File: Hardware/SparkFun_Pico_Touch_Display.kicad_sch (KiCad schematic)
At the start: 53 parts, among them J1 Conn_01x20, J2 Conn_01x20, J3 Conn_02x10_SMD_RA, J4 Conn_1x21_FPC, J5 Qwiic_Vertical, J6 microSD, Q1 RE1C002UNTCL, SW1 SMD_4.6x2.8mm_h2.5mm, U1 2" LCD-TFT 240x320, U2 PCA9554PW

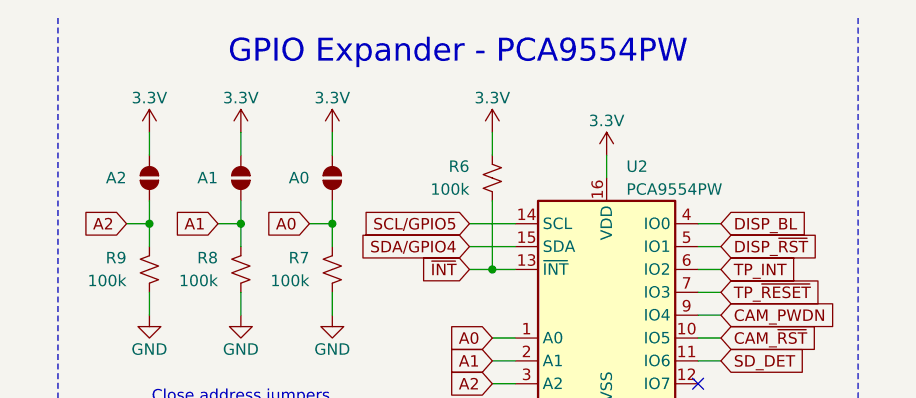
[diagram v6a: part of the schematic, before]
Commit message: Change GPIO expander to PCA9534
PCA9554 has internal pull-up resistors on IO pins, whereas PCA9534 does not. The pull-up resistors were causing problems with the camera not being enabled by default, so this will ensure the camera's pull-up/down resistors take priority.
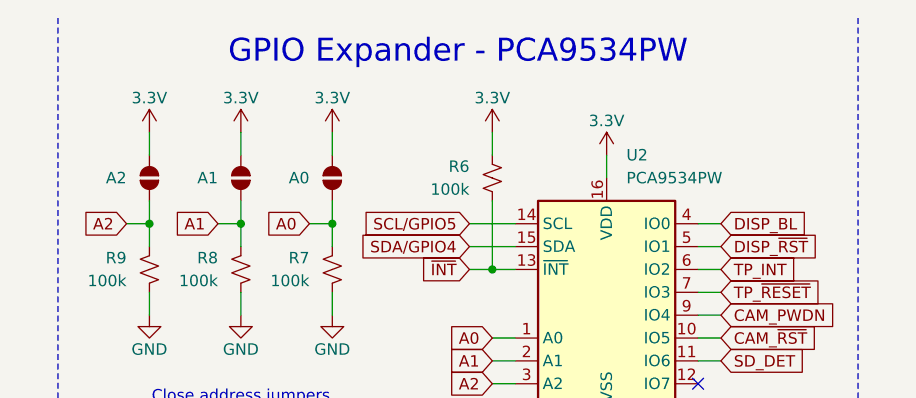
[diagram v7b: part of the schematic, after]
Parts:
- U2: value PCA9554PW -> PCA9534PW; symbol SparkFun-IC-Special-Function:PCA9554PW -> SparkFun-IC-Special-Function:PCA9534PW; PROD_ID IC-23589 -> IC-26490
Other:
- note added: "GPIO Expander - PCA9534PW"
- note removed: "GPIO Expander - PCA9554PW"
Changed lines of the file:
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@@
 		)
 	)
-	(text "GPIO Expander - PCA9554PW"
+	(text "GPIO Expander - PCA9534PW"
 		(exclude_from_sim no)
 		(at 146.05 16.51 0)
@@
 	)
 	(symbol
-		(lib_id "SparkFun-IC-Special-Function:PCA9554PW")
+		(lib_id "SparkFun-IC-Special-Function:PCA9534PW")
 		(at 162.56 43.18 0)
 		(unit 1)
@@
 		(fields_autoplaced yes)
 		(property "Reference" "U2"
-			(at 164.7541 29.21 0)
-			(effects
-				(font
-					(size 1.27 1.27)
-				)
-				(justify left)
-			)
-		)
-		(property "Value" "PCA9554PW"
-			(at 164.7541 31.75 0)
+			(at 164.7541 27.94 0)
+			(effects
+				(font
+					(size 1.27 1.27)
+				)
+				(justify left)
+			)
+		)
+		(property "Value" "PCA9534PW"
+			(at 164.7541 30.48 0)
 			(effects
 				(font
@@
 			)
 		)
-		(property "Datasheet" "https://www.ti.com/lit/ds/symlink/tca9554.pdf"
+		(property "Datasheet" "https://www.ti.com/lit/ds/symlink/tca9534.pdf"
 			(at 162.56 64.135 0)
 			(effects
@@
 			)
 		)
-		(property "PROD_ID" "IC-23589"
+		(property "PROD_ID" "IC-26490"
 			(at 162.56 66.675 0)
 			(effects
